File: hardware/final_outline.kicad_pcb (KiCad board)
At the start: 2 copper layers, 99.5 x 75 mm, 46 parts, among them P001 CANCONNECTOR, P002 CONN_01X14, P100 ISP, P101 DEBUG_LED, U401 MCP2551-I/SN, U403 LPC11C14, U501 MCP1755-33, U502 MCP1755-5, U6 TCA9543A, U7 LTC2943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

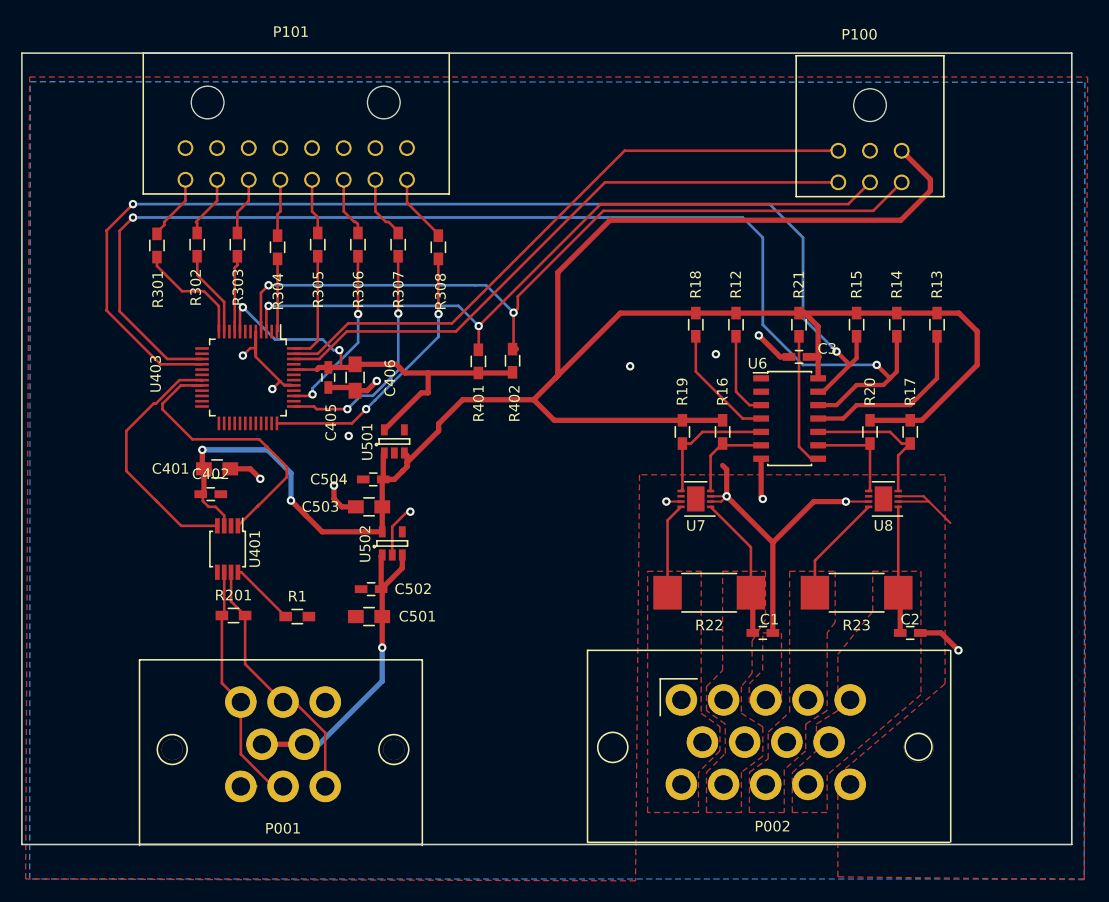
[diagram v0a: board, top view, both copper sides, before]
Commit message: Fixed connector zone spacing, added vias to back plate.
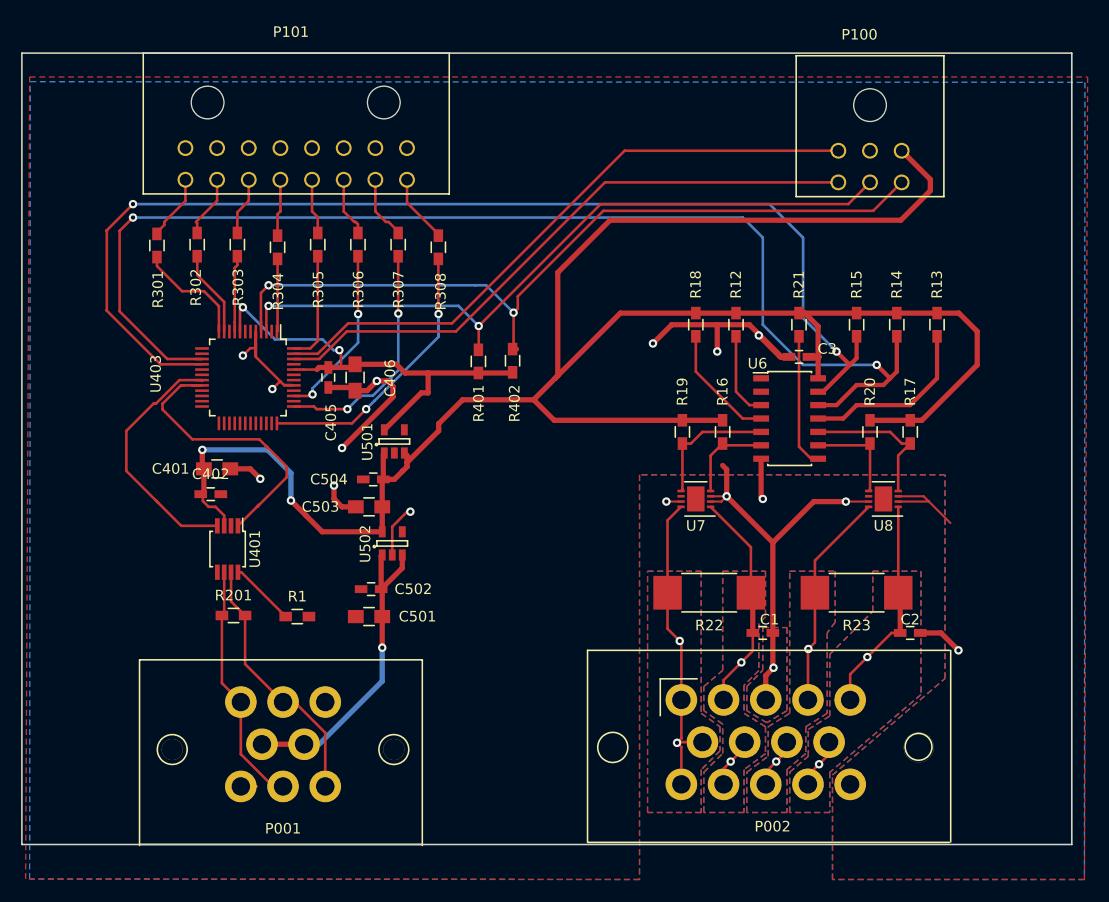
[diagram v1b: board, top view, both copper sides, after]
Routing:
- net GND: track 84.0 -> 117.7 mm, vias 12 -> 16
- net /BACK_PANEL/CS_SENSE-: track 10.3 -> 31.7 mm, vias 0 -> 2
- net /BACK_PANEL/LV_SENSE-: track 10.2 -> 25.5 mm, vias 0 -> 2
- net /BACK_PANEL/LV_SENSE+: track 12.0 -> 25.7 mm, vias 0 -> 2
- net /BACK_PANEL/CS_SENSE+: track 13.6 -> 25.9 mm, vias 0 -> 2
- net (no net): vias 3 -> 0
- added copper zone on B.Cu, net /BACK_PANEL/CS_SENSE+
- added copper zone on B.Cu, net /BACK_PANEL/LV_SENSE+
- added copper zone on B.Cu, net /BACK_PANEL/LV_SENSE-
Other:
- net class Default: clearance 0.13 -> 0.2
- net class POWER: clearance 0.13 -> 0.2
- rule trace_clearance: 0.13 -> 0.2

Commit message: Cleaned up PCB, changed via/zone spacings.
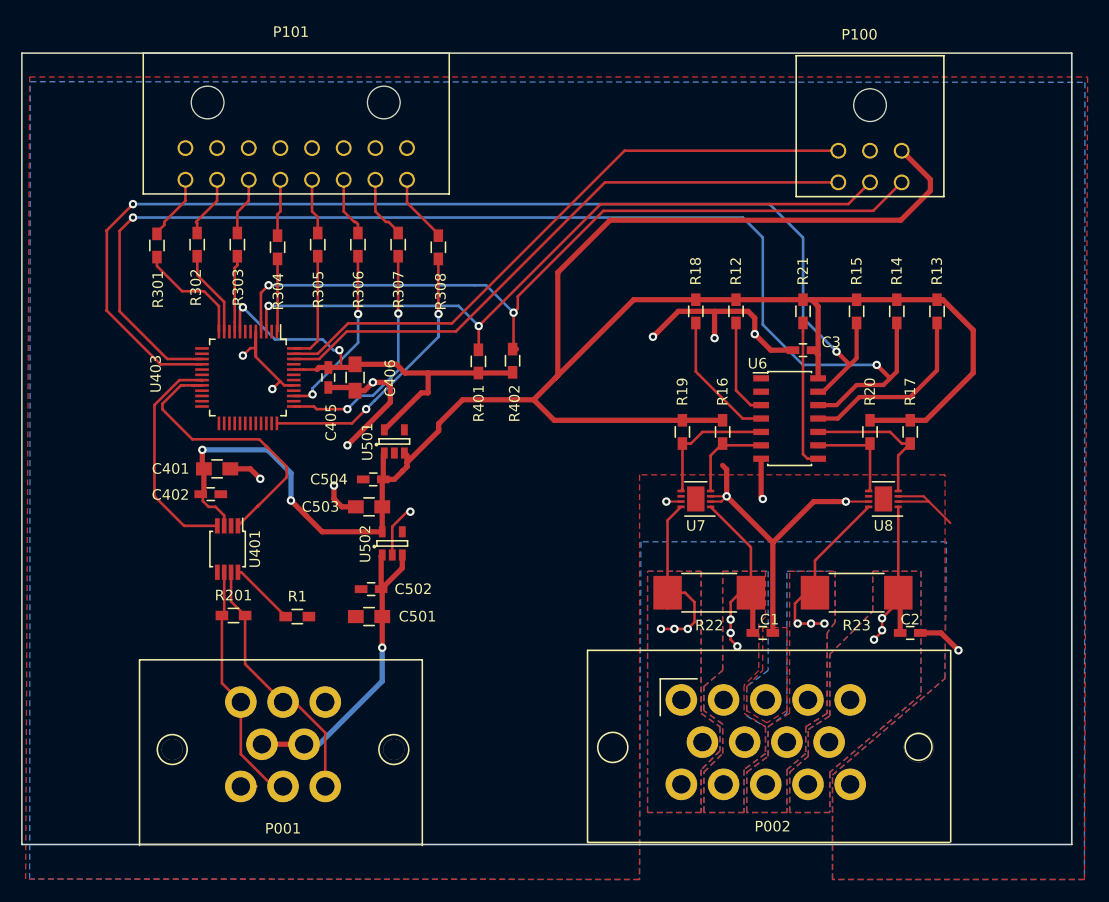
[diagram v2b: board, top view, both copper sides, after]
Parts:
- moved R21 1.33 mm to (176.5, 77.5)
- moved R12 1.27 mm to (170.2, 77.5)
- moved R13 1.27 mm to (189.2, 77.5)
- moved R14 1.27 mm to (185.4, 77.5)
- moved R15 1.27 mm to (181.6, 77.5)
- moved R18 1.27 mm to (166.4, 77.5)
- moved C3 0.74 mm to (176.5, 81.2)
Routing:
- net /BACK_PANEL/CS_SENSE-: track 31.7 -> 20.0 mm, vias 2 -> 3
- net GND: track 117.7 -> 108.2 mm, vias 16 -> 15
- net /BACK_PANEL/LV_SENSE-: track 25.5 -> 17.9 mm, vias 2 -> 3
- net /BACK_PANEL/LV_SENSE+: track 25.7 -> 18.6 mm, vias 2 -> 3
- net /BACK_PANEL/CS_SENSE+: track 25.9 -> 21.6 mm, vias 2 -> 3
- net /Micro_Controller/CAN_RXD: track 24.2 -> 21.4 mm
- net Net-(R21-Pad2): track 12.6 -> 14.7 mm
- net +5V: track 198.5 -> 200.0 mm
- net Net-(R18-Pad2): track 11.4 -> 12.6 mm
- net /I2C Multiplexer and Gas Gauges/SDA: track 108.3 -> 109.5 mm
- net /I2C Multiplexer and Gas Gauges/SCL: track 114.1 -> 115.4 mm
- net Net-(R12-Pad2): track 8.16 -> 9.35 mm
- net Net-(R13-Pad2): track 17.0 -> 17.7 mm
- net (no net): track 0.63 -> 0.00 mm
- added copper zone on B.Cu, net /BACK_PANEL/CS_SENSE-
